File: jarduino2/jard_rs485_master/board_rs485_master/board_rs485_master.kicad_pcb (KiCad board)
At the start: 2 copper layers, 132.4 x 70.8 mm, 56 parts, among them J1 POWER_12V, J2 Log, J3 POWER_OYAS_12V, J4 BUS_OYAS, J5 Leds RGB, J6 Button, Q1 BPC_2N2222A, Q2 BPC_IPP034N03L, Q3 BC327, Q4 BC327, U1 RtcArduino, U2 BPC_Alim5V, U3 BPC_ESP8266-01_ESP-01, U4 BPC_Mod485, U5 LM1117DT-3.3

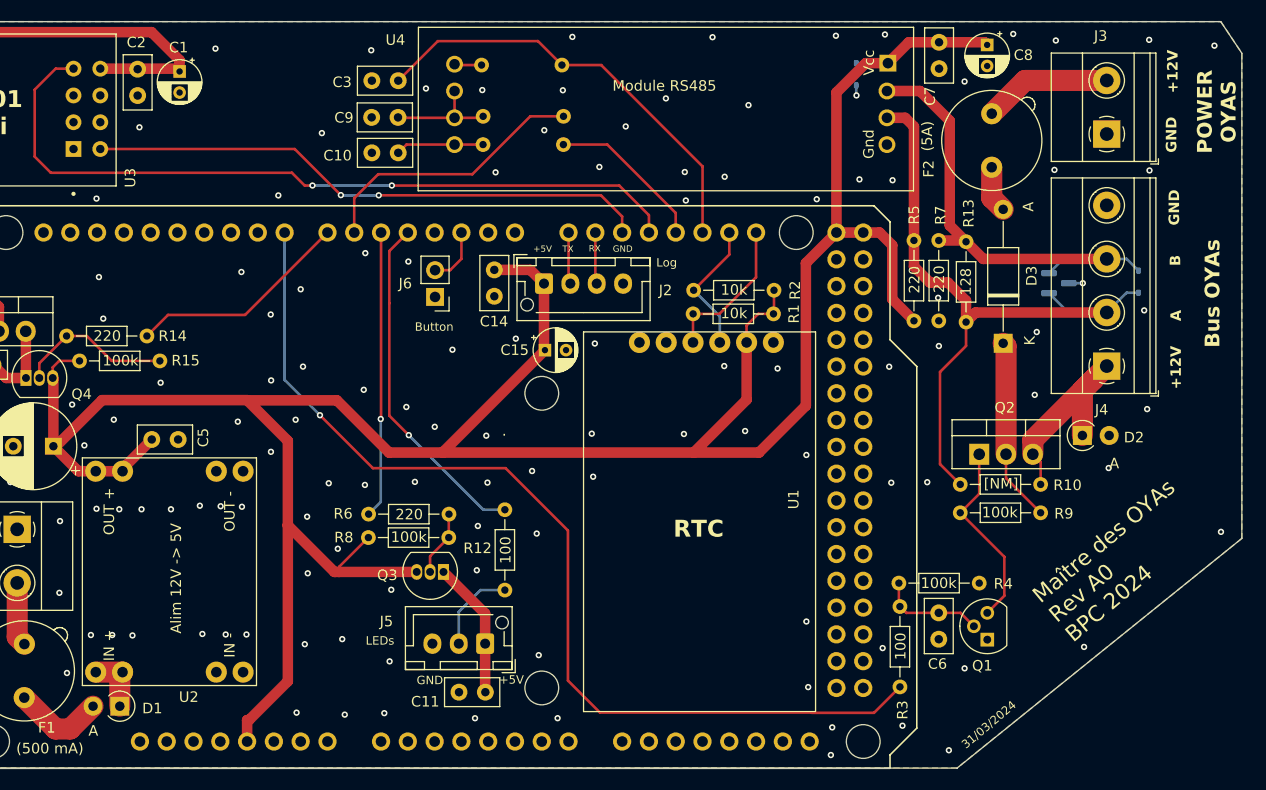
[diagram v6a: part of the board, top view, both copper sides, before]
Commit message: Amélioration suite remise en route:
  - Agrandissement trous des LEDs D1 et D3
  - Correction erreur type du MOS P GDS
  - Agrandissement empreintes de R5,R7,R13 et R10 + verticales
  - Ajout de la description des opérations de rework pour le MOD485
  - Ajout d'une interface pour adapter le bus (5V, A, B et Gnd)
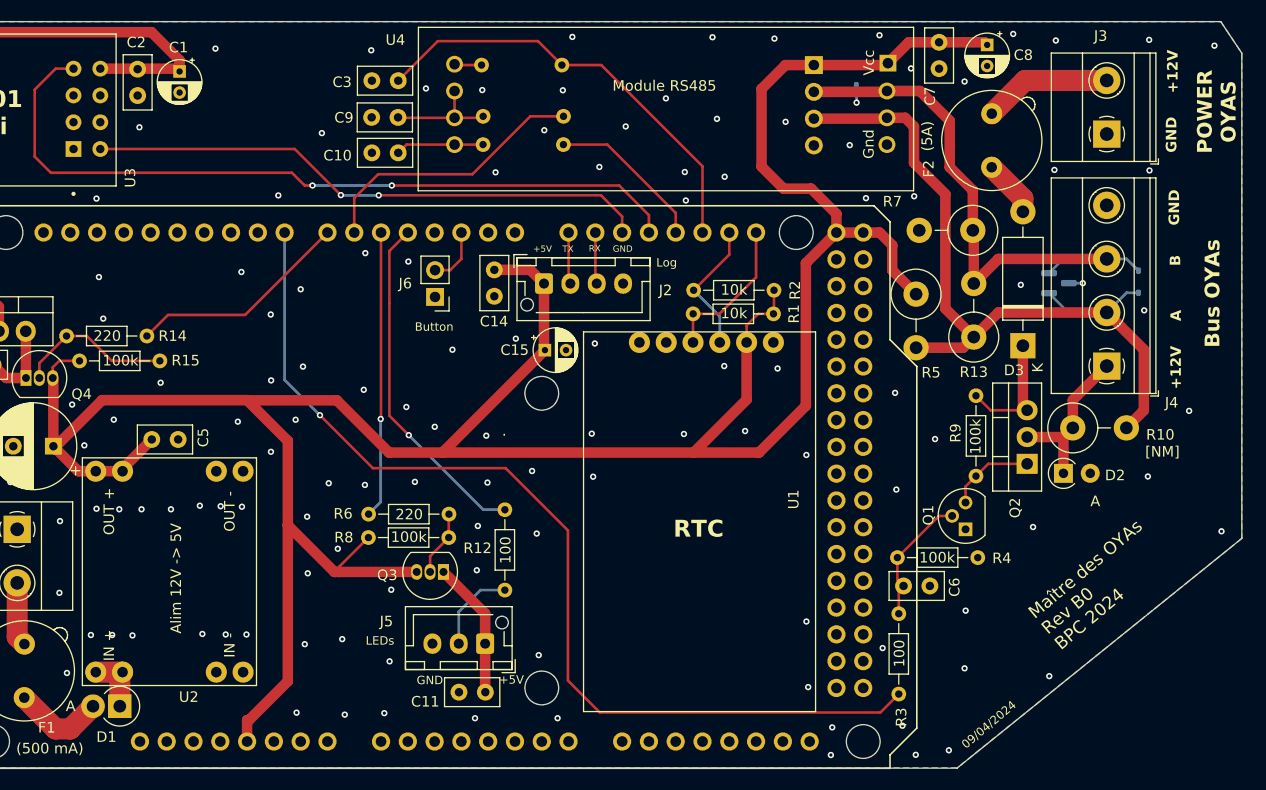
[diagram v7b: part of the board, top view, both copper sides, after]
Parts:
- added J7: Adapt BUS, Connector_PinHeader_2.54mm:PinHeader_1x04_P2.54mm_Vertical, B.Cu at (166.4, 53.1)
- D1: value D -> SR560; footprint Diode_THT:D_A-405_P2.54mm_Vertical_AnodeUp -> Diode_THT:D_DO-15_P2.54mm_Vertical_AnodeUp
- D2: value D -> BAT42
- D3: value D -> SR560; footprint Diode_THT:D_A-405_P12.70mm_Horizontal -> Diode_THT:D_DO-15_P12.70mm_Horizontal
- F1: value Fuse -> 500 mA
- F2: value Fuse -> 5A
- Q2: value BPC_IPP034N03L -> P03P4L-04
- R10, R13, R5, R7: footprint Resistor_THT:R_Axial_DIN0204_L3.6mm_D1.6mm_P7.62mm_Horizontal -> Resistor_THT:R_Axial_DIN0414_L11.9mm_D4.5mm_P5.08mm_Vertical
- moved R9 12.7 mm to (181.8, 84.5), turned to -90 degrees
- moved Q1 10.7 mm to (180.8, 97.1)
- moved R10 6.17 mm to (191.0, 87.5), turned to 0 degrees
- moved Q2 4.63 mm to (186.6, 90.9), turned to 90 degrees
- moved C6 4.20 mm to (174.9, 102.5), turned to 0 degrees
- moved D2 4.01 mm to (190.1, 91.8)
- moved R7 3.37 mm to (181.5, 68.8), turned to 180 degrees
- moved R5 2.54 mm to (176.1, 74.8), turned to -90 degrees
- moved R4 2.42 mm to (174.3, 99.8)
- moved D3 1.88 mm to (186.2, 79.7)
- moved R13 1.60 mm to (181.6, 78.9)
- moved R3 0.69 mm to (174.5, 105.1)
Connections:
- Q2 pad 2: Net-(D3-K) -> Net-(D2-K)
- Q2 pad 3: Net-(D2-K) -> Net-(D3-K)
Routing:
- net Net-(Q2-G): track 18.2 -> 8.25 mm
- net +5V: track 262.0 -> 271.3 mm
- net A: track 65.4 -> 74.7 mm
- net B: track 45.4 -> 53.5 mm
- net Net-(D3-K): track 17.5 -> 11.7 mm
- net Net-(D2-K): track 20.2 -> 15.3 mm
- net Net-(C6-Pad1): track 10.0 -> 12.6 mm
- net Net-(D3-A): track 4.44 -> 5.45 mm
- net GND: track 2.30 -> 2.98 mm, vias 136 -> 138
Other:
- board text added: "09/04/2024"
- board text added: "Maître des OYAs Rev B0 BPC 2024"
- board text removed: "31/03/2024"
- board text removed: "Maître des OYAs Rev A0 BPC 2024"

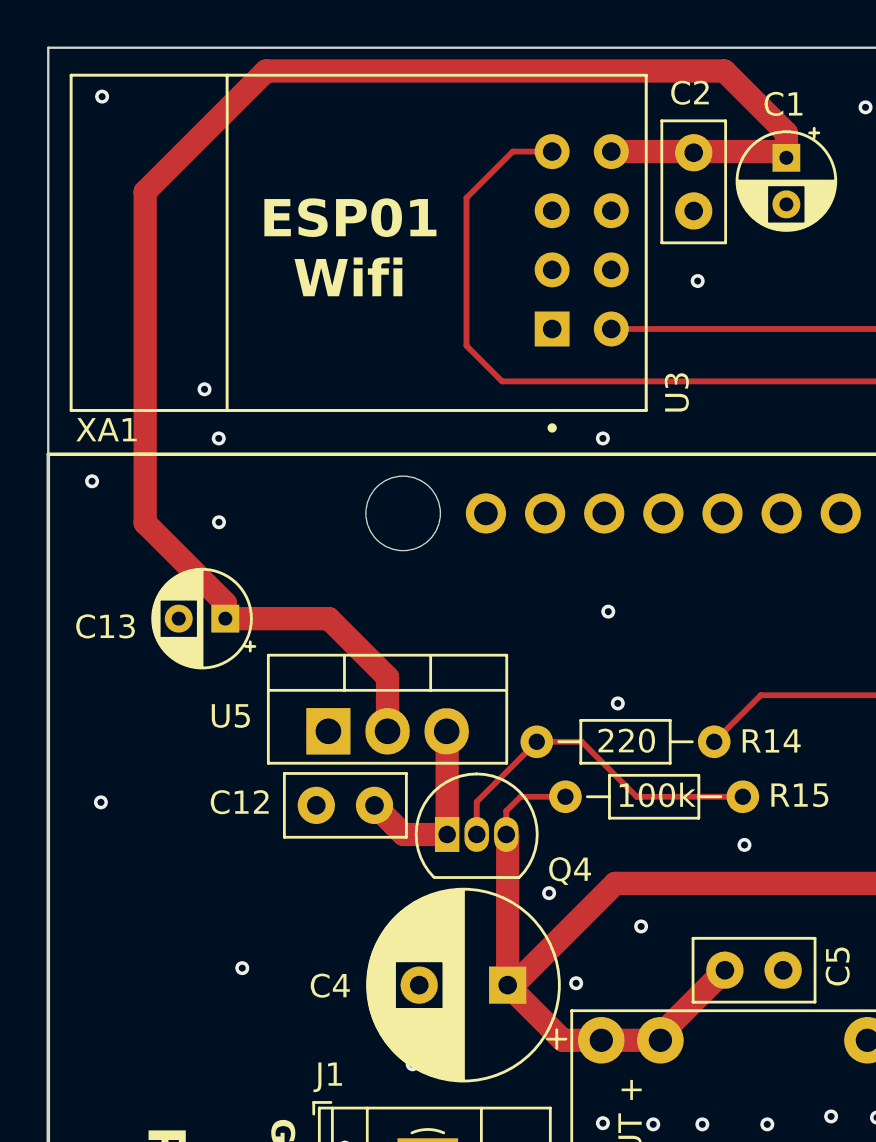
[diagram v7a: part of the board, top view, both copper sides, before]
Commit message: Déplacer C13 pour éviter le contact avec le port USB de la MEGA2460
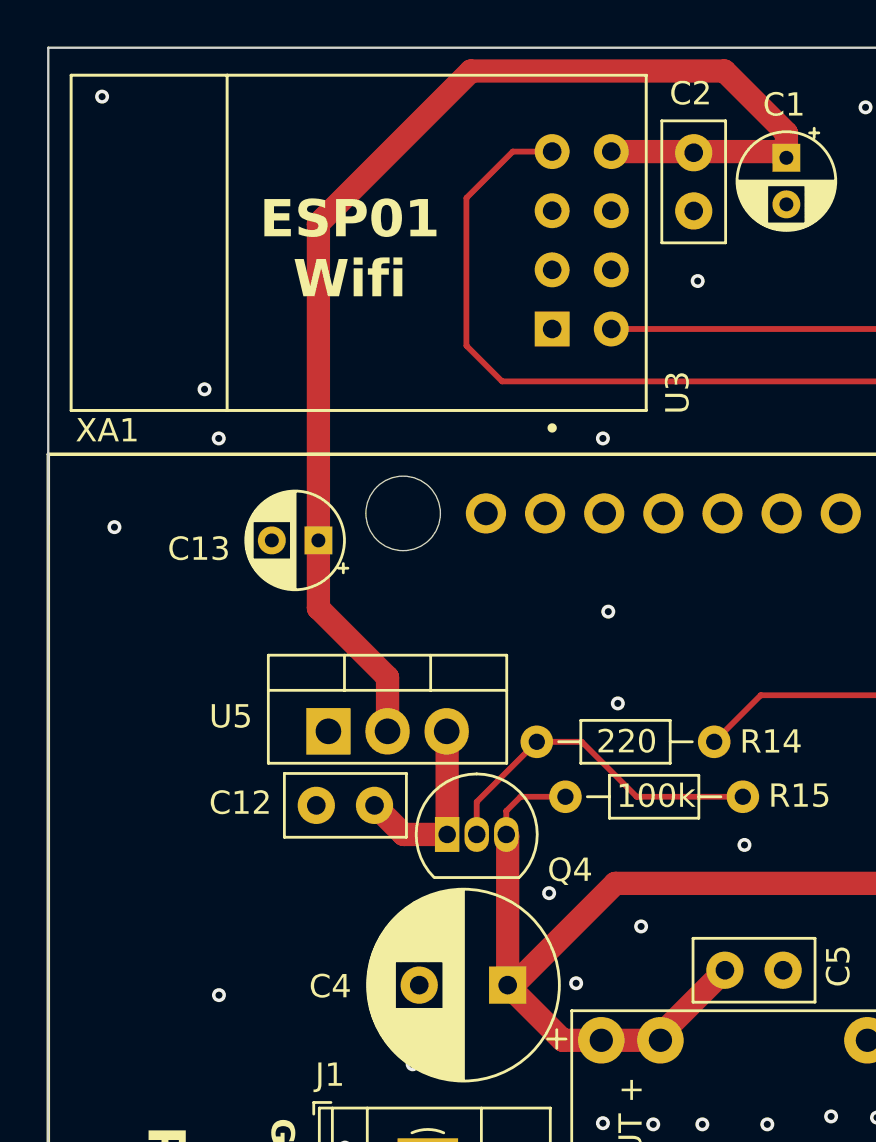
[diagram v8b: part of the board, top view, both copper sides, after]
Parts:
- moved C13 5.22 mm to (86.2, 70.2)
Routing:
- net POWER_3.3: track 69.6 -> 55.7 mm
- net GND: vias 138 -> 136
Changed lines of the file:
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@@
   )
   (footprint "Capacitor_THT:CP_Radial_D4.0mm_P2.00mm" (layer "F.Cu")
-    (at 82.1826 73.52 180)
+    (at 86.18 70.16 180)
     (descr "CP, Radial series, Radial, pin pitch=2.00mm, , diameter=4mm, Electrolytic Capacitor")
     (tags "CP Radial series Radial pin pitch 2.00mm  diameter 4mm Electrolytic Capacitor")
@@
   (via (at 142.12 115.05) (size 0.6) (drill 0.3) (layers "F.Cu" "B.Cu") (free) (net 2))
   (via (at 145.65 79.52) (size 0.6) (drill 0.3) (layers "F.Cu" "B.Cu") (free) (net 2))
-  (via (at 76.46 67.62) (size 0.6) (drill 0.3) (layers "F.Cu" "B.Cu") (free) (net 2))
+  (via (at 77.42 69.59) (size 0.6) (drill 0.3) (layers "F.Cu" "B.Cu") (free) (net 2))
   (via (at 112.14 72.74) (size 0.6) (drill 0.3) (layers "F.Cu" "B.Cu") (free) (net 2))
   (via (at 140.86 59.3) (size 0.6) (drill 0.3) (layers "F.Cu" "B.Cu") (free) (net 2))
@@
   (via (at 145.36 88.07) (size 0.6) (drill 0.3) (layers "F.Cu" "B.Cu") (free) (net 2))
   (via (at 114.94 89.79) (size 0.6) (drill 0.3) (layers "F.Cu" "B.Cu") (free) (net 2))
-  (via (at 76.84 81.41) (size 0.6) (drill 0.3) (layers "F.Cu" "B.Cu") (free) (net 2))
   (via (at 172.64 50.29) (size 0.6) (drill 0.3) (layers "F.Cu" "B.Cu") (free) (net 2))
   (via (at 121.7 107.55) (size 0.6) (drill 0.3) (layers "F.Cu" "B.Cu") (free) (net 2))
@@
   (via (at 140.33 109.07) (size 0.6) (drill 0.3) (layers "F.Cu" "B.Cu") (free) (net 2))
   (via (at 157.96 63.71) (size 0.6) (drill 0.3) (layers "F.Cu" "B.Cu") (free) (net 2))
-  (via (at 82.91 88.53) (size 0.6) (drill 0.3) (layers "F.Cu" "B.Cu") (free) (net 2))
+  (via (at 81.91 89.69) (size 0.6) (drill 0.3) (layers "F.Cu" "B.Cu") (free) (net 2))
   (via (at 157.92 81.66) (size 0.6) (drill 0.3) (layers "F.Cu" "B.Cu") (free) (net 2))
-  (via (at 81.91 69.38) (size 0.6) (drill 0.3) (layers "F.Cu" "B.Cu") (free) (net 2))
   (via (at 118.43 101.31) (size 0.6) (drill 0.3) (layers "F.Cu" "B.Cu") (free) (net 2))
   (via (at 165.88 112.1) (size 0.6) (drill 0.3) (layers "F.Cu" "B.Cu") (free) (net 2))
@@
   (segment (start 186.44 54.58) (end 183.29 57.73) (width 2) (layer "F.Cu") (net 96))
   (segment (start 194.19 54.58) (end 186.44 54.58) (width 2) (layer "F.Cu") (net 96))
+  (segment (start 89.15 76.04) (end 86.18 73.07) (width 1) (layer "F.Cu") (net 97))
   (segment (start 106.012599 53.46) (end 106.28 53.727401) (width 1) (layer "F.Cu") (net 97))
-  (segment (start 83.93 50) (end 78.74 55.19) (width 1) (layer "F.Cu") (net 97))
-  (segment (start 82.1826 73.52) (end 86.63 73.52) (width 1) (layer "F.Cu") (net 97))
-  (segment (start 89.15 76.04) (end 89.15 78.36) (width 1) (layer "F.Cu") (net 97))
-  (segment (start 78.74 55.19) (end 78.74 69.41) (width 1) (layer "F.Cu") (net 97))
-  (segment (start 86.63 73.52) (end 89.15 76.04) (width 1) (layer "F.Cu") (net 97))
-  (segment (start 103.62 50) (end 83.93 50) (width 1) (layer "F.Cu") (net 97))
+  (segment (start 89.15 78.36) (end 89.15 76.04) (width 1) (layer "F.Cu") (net 97))
+  (segment (start 103.62 50) (end 92.73 50) (width 1) (layer "F.Cu") (net 97))
+  (segment (start 86.18 56.55) (end 92.73 50) (width 1) (layer "F.Cu") (net 97))
+  (segment (start 86.18 70.16) (end 86.18 56.55) (width 1) (layer "F.Cu") (net 97))
+  (segment (start 86.18 73.07) (end 86.18 70.16) (width 1) (layer "F.Cu") (net 97))
   (segment (start 106.28 53.727401) (end 106.28 52.66) (width 1) (layer "F.Cu") (net 97))
   (segment (start 106.28 52.66) (end 103.62 50) (width 1) (layer "F.Cu") (net 97))
   (segment (start 98.76 53.46) (end 106.012599 53.46) (width 1) (layer "F.Cu") (net 97))
-  (segment (start 82.1826 72.8526) (end 78.74 69.41) (width 1) (layer "F.Cu") (net 97))
-  (segment (start 82.1826 73.52) (end 82.1826 72.8526) (width 1) (layer "F.Cu") (net 97))
   (segment (start 99.85 81.17) (end 97.49 78.81) (width 0.25) (layer "F.Cu") (net 98))
   (segment (start 97.49 78.81) (end 95.56 78.81) (width 0.25) (layer "F.Cu") (net 98))
